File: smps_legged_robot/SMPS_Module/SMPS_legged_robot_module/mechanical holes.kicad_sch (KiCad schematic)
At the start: 6 parts

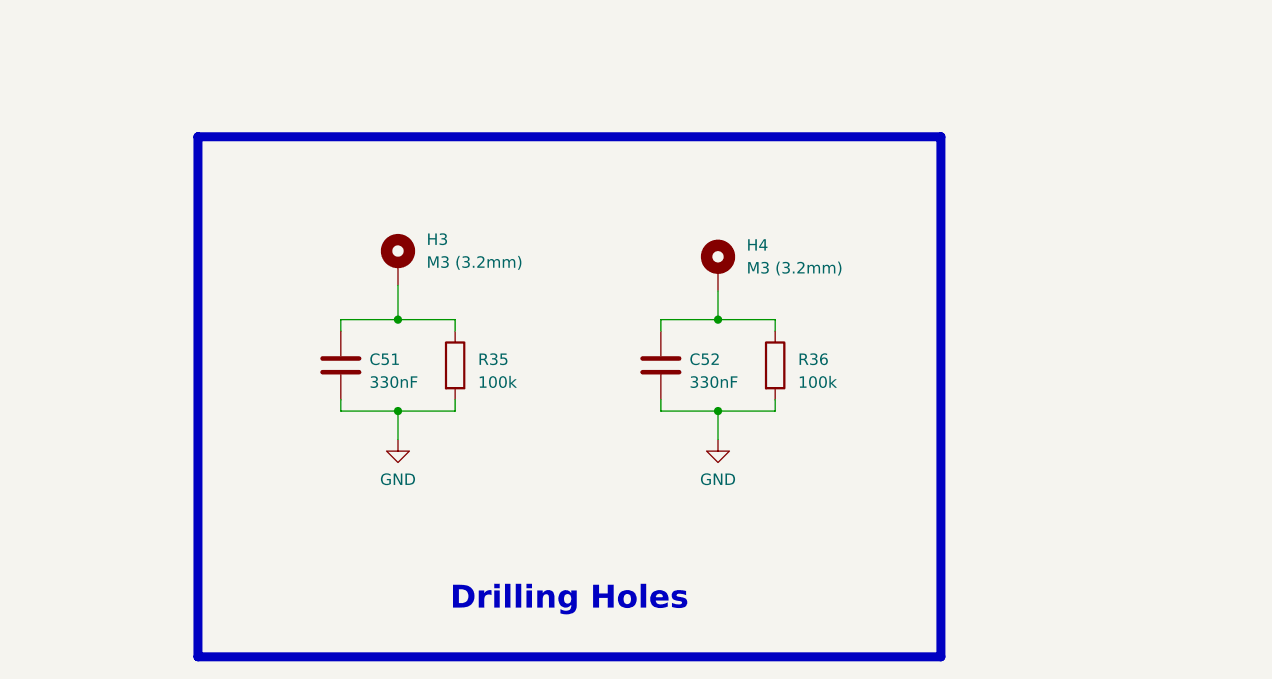
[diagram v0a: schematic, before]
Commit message: Buck module finished pending review
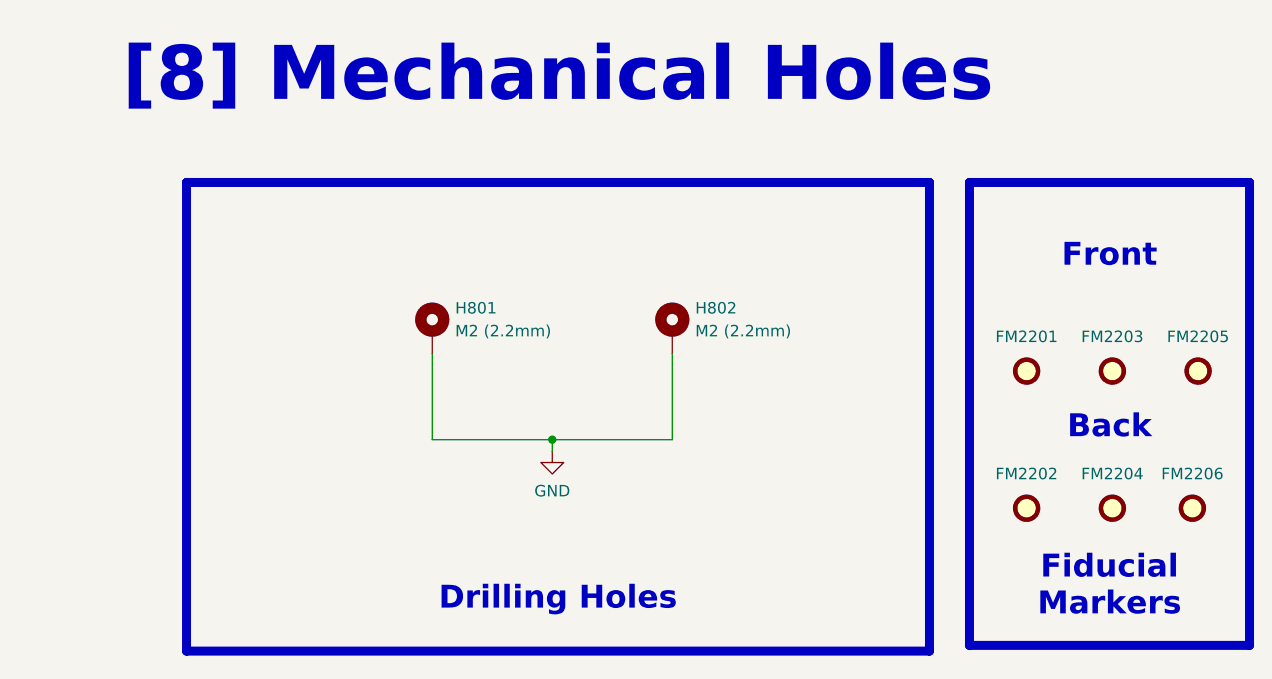
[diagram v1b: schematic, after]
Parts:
- removed C51, C52: 330nF, Capacitor_SMD:C_0603_1608Metric, symbol Device:C
- removed H3, H4: M3 (3.2mm), MountingHole:MountingHole_3.2mm_M3_Pad_Via, symbol Mechanical:MountingHole_Pad
- removed R35, R36: 100k, Resistor_SMD:R_0603_1608Metric, symbol Device:R
- added FM2201, FM2202, FM2203, FM2204, FM2205, FM2206: Fiducial, 0_fiducials:Fiducial_1mm_Mask2mm, symbol Mechanical:Fiducial
- added H801, H802: M2 (2.2mm), MountingHole:MountingHole_2.2mm_M2_Pad_Via, symbol Mechanical:MountingHole_Pad
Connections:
- net GND: now also H801.1, H802.1

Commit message: Correction module
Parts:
- renumbered FM2201 to FM701, FM2203 to FM702, FM2205 to FM703, FM2202 to FM704, FM2204 to FM705, FM2206 to FM706
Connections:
- net GND: no longer names the net of H801.1
- net GND: no longer H802.1
- no-connect marks 0 -> 2
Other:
- moved on the sheet: H801, H802
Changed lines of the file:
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@@
 (kicad_sch (version 20230121) (generator eeschema)
   (paper "A5")
-  (junction (at 104.775 61.595) (diameter 0) (color 0 0 0 0)
-  )
-  (wire (pts (xy 91.44 61.595) (xy 104.775 61.595))
-    (stroke (width 0) (type default))
-  )
-  (wire (pts (xy 91.44 52.07) (xy 91.44 61.595))
-    (stroke (width 0) (type default))
-  )
-  (wire (pts (xy 104.775 61.595) (xy 104.775 62.865))
-    (stroke (width 0) (type default))
-  )
-  (wire (pts (xy 104.775 61.595) (xy 118.11 61.595))
-    (stroke (width 0) (type default))
-  )
-  (wire (pts (xy 118.11 52.07) (xy 118.11 61.595))
-    (stroke (width 0) (type default))
-  )
+  (no_connect (at 89.535 57.785))
+  (no_connect (at 116.205 57.785))
   (rectangle (start 64.135 33.02) (end 146.685 85.09)
     (stroke (width 1) (type default) (color 200 200 200 1))
@@
   (symbol (lib_id "Mechanical:Fiducial") (at 157.48 69.215 0) (unit 1)
     (in_bom no) (on_board yes) (dnp no)
-    (property "Reference" "FM2202" (at 157.48 65.405 0)
+    (property "Reference" "FM704" (at 157.48 65.405 0)
       (effects (font (size 1.27 1.27)))
     )
@@
     )
   )
-  (symbol (lib_id "Mechanical:MountingHole_Pad") (at 91.44 49.53 0) (unit 1)
+  (symbol (lib_id "Mechanical:MountingHole_Pad") (at 89.535 55.245 0) (unit 1)
     (in_bom no) (on_board yes) (dnp no) (fields_autoplaced)
-    (property "Reference" "H801" (at 93.98 46.99 0)
-      (effects (font (size 1.27 1.27)) (justify left))
-    )
-    (property "Value" "M2 (2.2mm)" (at 93.98 49.53 0)
-      (effects (font (size 1.27 1.27)) (justify left))
-    )
-    (property "Footprint" "MountingHole:MountingHole_2.2mm_M2_Pad_Via" (at 91.44 49.53 0)
-      (effects (font (size 1.27 1.27)) hide)
-    )
-    (property "Datasheet" "~" (at 91.44 49.53 0)
+    (property "Reference" "H801" (at 92.075 52.705 0)
+      (effects (font (size 1.27 1.27)) (justify left))
+    )
+    (property "Value" "M2 (2.2mm)" (at 92.075 55.245 0)
+      (effects (font (size 1.27 1.27)) (justify left))
+    )
+    (property "Footprint" "MountingHole:MountingHole_2.2mm_M2_Pad_Via" (at 89.535 55.245 0)
+      (effects (font (size 1.27 1.27)) hide)
+    )
+    (property "Datasheet" "~" (at 89.535 55.245 0)
       (effects (font (size 1.27 1.27)) hide)
     )
@@
   (symbol (lib_id "Mechanical:Fiducial") (at 167.005 53.975 0) (unit 1)
     (in_bom no) (on_board yes) (dnp no)
-    (property "Reference" "FM2203" (at 167.005 50.165 0)
+    (property "Reference" "FM702" (at 167.005 50.165 0)
       (effects (font (size 1.27 1.27)))
     )
@@
   (symbol (lib_id "Mechanical:Fiducial") (at 157.48 53.975 0) (unit 1)
     (in_bom no) (on_board yes) (dnp no)
-    (property "Reference" "FM2201" (at 157.48 50.165 0)
+    (property "Reference" "FM701" (at 157.48 50.165 0)
       (effects (font (size 1.27 1.27)))
     )
@@
     )
   )
-  (symbol (lib_id "Mechanical:MountingHole_Pad") (at 118.11 49.53 0) (unit 1)
+  (symbol (lib_id "Mechanical:MountingHole_Pad") (at 116.205 55.245 0) (unit 1)
     (in_bom no) (on_board yes) (dnp no) (fields_autoplaced)
-    (property "Reference" "H802" (at 120.65 46.99 0)
-      (effects (font (size 1.27 1.27)) (justify left))
-    )
-    (property "Value" "M2 (2.2mm)" (at 120.65 49.53 0)
-      (effects (font (size 1.27 1.27)) (justify left))
-    )
-    (property "Footprint" "MountingHole:MountingHole_2.2mm_M2_Pad_Via" (at 118.11 49.53 0)
-      (effects (font (size 1.27 1.27)) hide)
-    )
-    (property "Datasheet" "~" (at 118.11 49.53 0)
+    (property "Reference" "H802" (at 118.745 52.705 0)
+      (effects (font (size 1.27 1.27)) (justify left))
+    )
+    (property "Value" "M2 (2.2mm)" (at 118.745 55.245 0)
+      (effects (font (size 1.27 1.27)) (justify left))
+    )
+    (property "Footprint" "MountingHole:MountingHole_2.2mm_M2_Pad_Via" (at 116.205 55.245 0)
+      (effects (font (size 1.27 1.27)) hide)
+    )
+    (property "Datasheet" "~" (at 116.205 55.245 0)
       (effects (font (size 1.27 1.27)) hide)
     )
@@
     )
   )
-  (symbol (lib_id "power:GND") (at 104.775 62.865 0) (unit 1)
-    (in_bom yes) (on_board yes) (dnp no) (fields_autoplaced)
-    (property "Reference" "#PWR0801" (at 104.775 69.215 0)
-      (effects (font (size 1.27 1.27)) hide)
-    )
-    (property "Value" "GND" (at 104.775 67.31 0)
-      (effects (font (size 1.27 1.27)))
-    )
-    (property "Footprint" "" (at 104.775 62.865 0)
-      (effects (font (size 1.27 1.27)) hide)
-    )
-    (property "Datasheet" "" (at 104.775 62.865 0)
-      (effects (font (size 1.27 1.27)) hide)
-    )
-    (pin "1")
-    (instances
-      (project "SMPS_legged_robot_module"
-        (path "/0650c7a8-acba-429c-9f8e-eec0baf0bc1c/fede4c36-00cc-4d3d-b71c-5243ba232202/1dbdd458-9c8a-4b0b-ac5b-dcf9040035b1"
-          (reference "#PWR0801") (unit 1)
-        )
-      )
-      (project "nav_lower_controller"
-        (path "/c33f1911-8ce0-4760-84e8-8afddd8478b5/943f81db-0df7-42f2-902e-793eba68ba4d"
-          (reference "#PWR023") (unit 1)
-        )
-      )
-      (project "nav_controller_interface_v2"
-        (path "/f0803068-2e71-498b-a1b0-83a54c15ca3c/34a10433-46e4-4cde-811a-979db0467e4a"
-          (reference "#PWR0501") (unit 1)
-        )
-      )
-    )
-  )
   (symbol (lib_id "Mechanical:Fiducial") (at 175.895 69.215 0) (unit 1)
     (in_bom no) (on_board yes) (dnp no)
-    (property "Reference" "FM2206" (at 175.895 65.405 0)
+    (property "Reference" "FM706" (at 175.895 65.405 0)
       (effects (font (size 1.27 1.27)))
     )
@@
   (symbol (lib_id "Mechanical:Fiducial") (at 176.53 53.975 0) (unit 1)
     (in_bom no) (on_board yes) (dnp no)
-    (property "Reference" "FM2205" (at 176.53 50.165 0)
+    (property "Reference" "FM703" (at 176.53 50.165 0)
       (effects (font (size 1.27 1.27)))
     )
@@
   (symbol (lib_id "Mechanical:Fiducial") (at 167.005 69.215 0) (unit 1)
     (in_bom no) (on_board yes) (dnp no)
-    (property "Reference" "FM2204" (at 167.005 65.405 0)
-      (effects (font (size 1.27 1.27)))
-    )
+    (property "Reference" "FM705" (at 167.005 65.405 0)
+      (effects (font (size 1.27 1.27)))
+    )
